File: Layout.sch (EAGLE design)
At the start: 1 part

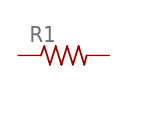
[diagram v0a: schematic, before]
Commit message: Added resistor value to R1
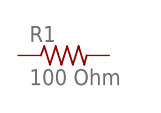
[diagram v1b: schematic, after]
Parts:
- R1: value (none) -> 100 Ohm
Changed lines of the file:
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@@
 </classes>
 <parts>
-<part name="R1" library="rcl" deviceset="R-US_" device="0204/2V"/>
+<part name="R1" library="rcl" deviceset="R-US_" device="0204/2V" value="100 Ohm"/>
 </parts>
 <sheets>

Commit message: Initial Python interface to Eagle 6 files
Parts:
- added U$1: BEAGLEBOARD, mecanum-symbols:BEAGLEBOARD
- added U1: ARDUINO-MEGAFULL, SparkFun-Boards:ARDUINO-MEGAFULL
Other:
- moved on the sheet: R1
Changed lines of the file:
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@@
 <layer number="48" name="Document" color="7" fill="1" visible="no" active="no"/>
 <layer number="49" name="Reference" color="7" fill="1" visible="no" active="no"/>
+<layer number="50" name="dxf" color="7" fill="1" visible="no" active="no"/>
 <layer number="51" name="tDocu" color="6" fill="1" visible="no" active="no"/>
 <layer number="52" name="bDocu" color="7" fill="1" visible="no" active="no"/>
+<layer number="53" name="tGND_GNDA" color="7" fill="9" visible="no" active="no"/>
+<layer number="54" name="bGND_GNDA" color="1" fill="9" visible="no" active="no"/>
+<layer number="56" name="wert" color="7" fill="1" visible="no" active="no"/>
 <layer number="91" name="Nets" color="2" fill="1" visible="yes" active="yes"/>
 <layer number="92" name="Busses" color="1" fill="1" visible="yes" active="yes"/>
@@
 <layer number="97" name="Info" color="7" fill="1" visible="yes" active="yes"/>
 <layer number="98" name="Guide" color="6" fill="1" visible="yes" active="yes"/>
+<layer number="100" name="Muster" color="7" fill="1" visible="no" active="no"/>
+<layer number="101" name="Patch_Top" color="12" fill="4" visible="no" active="yes"/>
+<layer number="102" name="Vscore" color="7" fill="1" visible="no" active="yes"/>
+<layer number="103" name="tMap" color="7" fill="1" visible="no" active="yes"/>
+<layer number="104" name="Name" color="16" fill="1" visible="no" active="yes"/>
+<layer number="105" name="tPlate" color="7" fill="1" visible="no" active="yes"/>
+<layer number="106" name="bPlate" color="7" fill="1" visible="no" active="yes"/>
+<layer number="107" name="Crop" color="7" fill="1" visible="no" active="yes"/>
+<layer number="116" name="Patch_BOT" color="9" fill="4" visible="no" active="yes"/>
+<layer number="121" name="_tsilk" color="7" fill="1" visible="no" active="yes"/>
+<layer number="122" name="_bsilk" color="7" fill="1" visible="no" active="yes"/>
+<layer number="125" name="_tNames" color="7" fill="1" visible="no" active="yes"/>
+<layer number="144" name="Drill_legend" color="7" fill="1" visible="no" active="yes"/>
+<layer number="151" name="HeatSink" color="7" fill="1" visible="no" active="yes"/>
+<layer number="200" name="200bmp" color="1" fill="10" visible="no" active="yes"/>
+<layer number="201" name="201bmp" color="2" fill="10" visible="no" active="yes"/>
+<layer number="202" name="202bmp" color="3" fill="10" visible="no" active="yes"/>
+<layer number="203" name="203bmp" color="4" fill="10" visible="no" active="yes"/>
+<layer number="204" name="204bmp" color="5" fill="10" visible="no" active="yes"/>
+<layer number="205" name="205bmp" color="6" fill="10" visible="no" active="yes"/>
+<layer number="206" name="206bmp" color="7" fill="10" visible="no" active="yes"/>
+<layer number="207" name="207bmp" color="8" fill="10" visible="no" active="yes"/>
+<layer number="208" name="208bmp" color="9" fill="10" visible="no" active="yes"/>
+<layer number="209" name="209bmp" color="7" fill="1" visible="no" active="yes"/>
+<layer number="210" name="210bmp" color="7" fill="1" visible="no" active="yes"/>
+<layer number="211" name="211bmp" color="7" fill="1" visible="no" active="yes"/>
+<layer number="212" name="212bmp" color="7" fill="1" visible="no" active="yes"/>
+<layer number="213" name="213bmp" color="7" fill="1" visible="no" active="yes"/>
+<layer number="214" name="214bmp" color="7" fill="1" visible="no" active="yes"/>
+<layer number="215" name="215bmp" color="7" fill="1" visible="no" active="yes"/>
+<layer number="216" name="216bmp" color="7" fill="1" visible="no" active="yes"/>
+<layer number="217" name="217bmp" color="18" fill="1" visible="no" active="no"/>
+<layer number="218" name="218bmp" color="19" fill="1" visible="no" active="no"/>
+<layer number="219" name="219bmp" color="20" fill="1" visible="no" active="no"/>
+<layer number="220" name="220bmp" color="21" fill="1" visible="no" active="no"/>
+<layer number="221" name="221bmp" color="22" fill="1" visible="no" active="no"/>
+<layer number="222" name="222bmp" color="23" fill="1" visible="no" active="no"/>
+<layer number="223" name="223bmp" color="24" fill="1" visible="no" active="no"/>
+<layer number="224" name="224bmp" color="25" fill="1" visible="no" active="no"/>
+<layer number="250" name="Descript" color="3" fill="1" visible="no" active="no"/>
+<layer number="251" name="SMDround" color="12" fill="11" visible="no" active="no"/>
+<layer number="254" name="cooling" color="7" fill="1" visible="no" active="yes"/>
 </layers>
 <schematic xreflabel="%F%N/%S.%C%R" xrefpart="/%S.%C%R">
@@
 <parts>
 <part name="R1" library="rcl" deviceset="R-US_" device="0204/2V" value="100 Ohm"/>
+<part name="U1" library="SparkFun-Boards" deviceset="ARDUINO-MEGA" device="FULL"/>
+<part name="U$1" library="mecanum-symbols" deviceset="BEAGLEBOARD" device=""/>
 </parts>
 <sheets>
@@
 </plain>
 <instances>
-<instance part="R1" gate="G$1" x="22.86" y="22.86"/>
+<instance part="R1" gate="G$1" x="12.7" y="10.16"/>
+<instance part="U1" gate="G$1" x="-43.18" y="12.7"/>
+<instance part="U$1" gate="G$1" x="66.04" y="25.4"/>
 </instances>
 <busses>
